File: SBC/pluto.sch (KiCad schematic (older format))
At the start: 0 parts

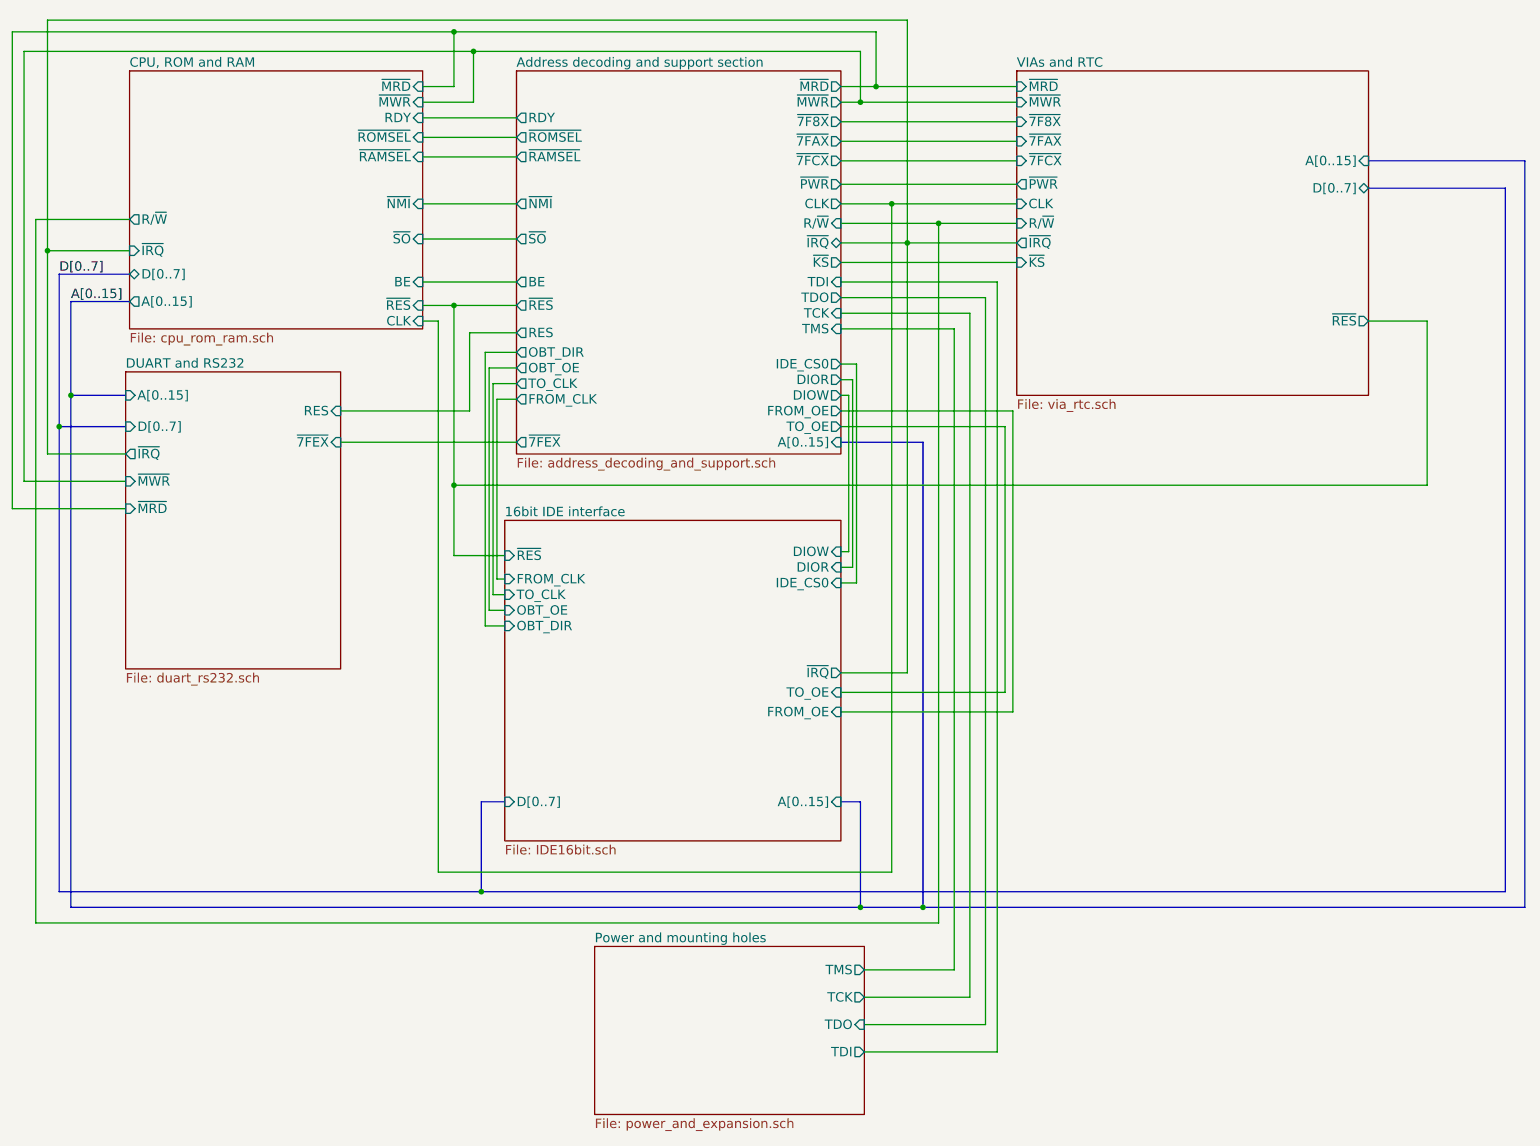
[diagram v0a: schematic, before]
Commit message: Board ready for production. Added a reset IC that does both low and high logic RES. A power switch and fuse holder is in place. The expansion bus is back, but with an IDC 40 pin connector.
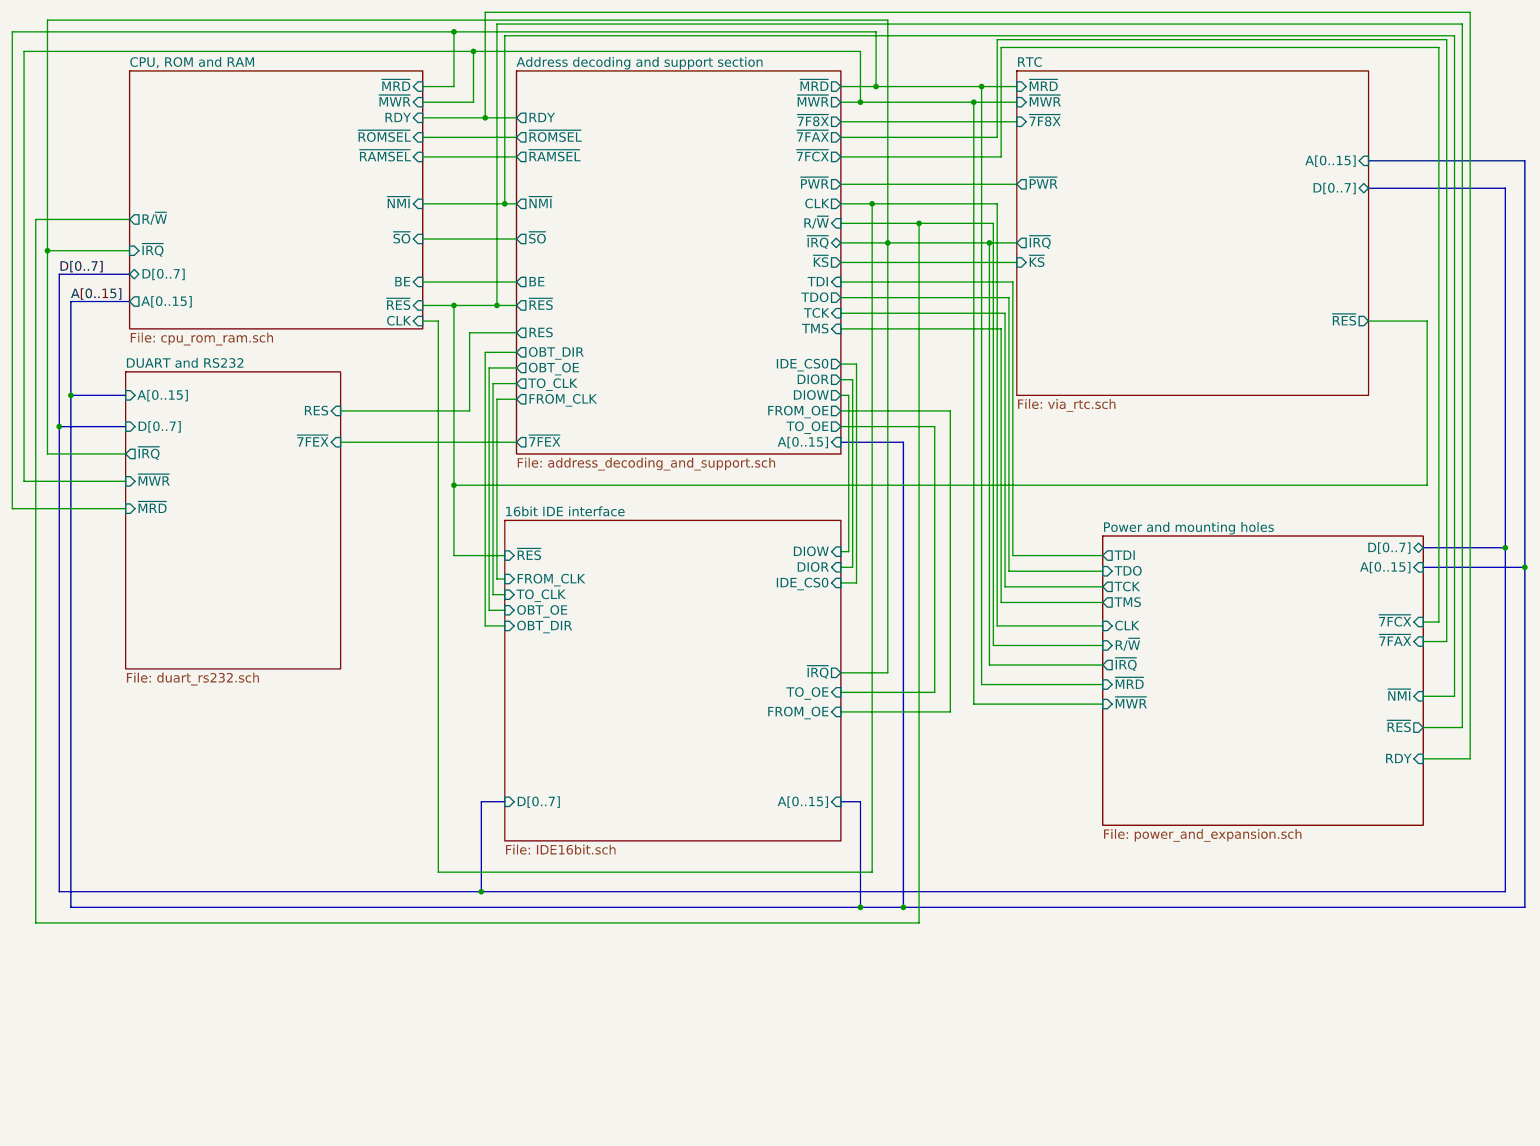
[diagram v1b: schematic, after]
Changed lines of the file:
@@
 LIBS:transistor
 LIBS:uln-ic
+LIBS:74xgxx
+LIBS:ac-dc
+LIBS:actel
+LIBS:allegro
+LIBS:Altera
+LIBS:analog_devices
+LIBS:battery_management
+LIBS:bbd
+LIBS:bosch
+LIBS:brooktre
+LIBS:cmos_ieee
+LIBS:dc-dc
+LIBS:diode
+LIBS:elec-unifil
+LIBS:ESD_Protection
+LIBS:ftdi
+LIBS:gennum
+LIBS:graphic
+LIBS:hc11
+LIBS:intersil
+LIBS:ir
+LIBS:Lattice
+LIBS:leds
+LIBS:LEM
+LIBS:logo
+LIBS:maxim
+LIBS:mechanical
+LIBS:microchip_dspic33dsc
+LIBS:microchip_pic10mcu
+LIBS:microchip_pic12mcu
+LIBS:microchip_pic16mcu
+LIBS:microchip_pic18mcu
+LIBS:microchip_pic24mcu
+LIBS:microchip_pic32mcu
+LIBS:modules
+LIBS:motor_drivers
+LIBS:motors
+LIBS:msp430
+LIBS:nordicsemi
+LIBS:nxp
+LIBS:nxp_armmcu
+LIBS:onsemi
+LIBS:Oscillators
+LIBS:powerint
+LIBS:Power_Management
+LIBS:pspice
+LIBS:references
+LIBS:relays
+LIBS:rfcom
+LIBS:RFSolutions
+LIBS:sensors
+LIBS:silabs
+LIBS:stm8
+LIBS:stm32
+LIBS:supertex
+LIBS:switches
+LIBS:transf
+LIBS:triac_thyristor
+LIBS:ttl_ieee
+LIBS:video
+LIBS:wiznet
+LIBS:Worldsemi
+LIBS:Xicor
+LIBS:zetex
+LIBS:Zilog
+LIBS:pluto
 LIBS:+1.8V
 LIBS:+3.3V
@@
 LIBS:VREG
 LIBS:VREG_VOUTCENTER
-LIBS:74xgxx
-LIBS:ac-dc
-LIBS:actel
-LIBS:allegro
-LIBS:Altera
-LIBS:analog_devices
-LIBS:battery_management
-LIBS:bbd
-LIBS:bosch
-LIBS:brooktre
-LIBS:cmos_ieee
-LIBS:dc-dc
-LIBS:diode
-LIBS:elec-unifil
-LIBS:ESD_Protection
-LIBS:ftdi
-LIBS:gennum
-LIBS:graphic
-LIBS:hc11
-LIBS:intersil
-LIBS:ir
-LIBS:Lattice
-LIBS:leds
-LIBS:LEM
-LIBS:logo
-LIBS:maxim
-LIBS:mechanical
-LIBS:microchip_dspic33dsc
-LIBS:microchip_pic10mcu
-LIBS:microchip_pic12mcu
-LIBS:microchip_pic16mcu
-LIBS:microchip_pic18mcu
-LIBS:microchip_pic24mcu
-LIBS:microchip_pic32mcu
-LIBS:modules
-LIBS:motor_drivers
-LIBS:motors
-LIBS:msp430
-LIBS:nordicsemi
-LIBS:nxp
-LIBS:nxp_armmcu
-LIBS:onsemi
-LIBS:Oscillators
-LIBS:powerint
-LIBS:Power_Management
-LIBS:pspice
-LIBS:references
-LIBS:relays
-LIBS:rfcom
-LIBS:RFSolutions
-LIBS:sensors
-LIBS:silabs
-LIBS:stm8
-LIBS:stm32
-LIBS:supertex
-LIBS:switches
-LIBS:transf
-LIBS:triac_thyristor
-LIBS:ttl_ieee
-LIBS:video
-LIBS:wiznet
-LIBS:Worldsemi
-LIBS:Xicor
-LIBS:zetex
-LIBS:Zilog
-LIBS:pluto
 LIBS:pluto-cache
 EELAYER 25 0
@@
 S 7025 900  2250 2075
 U 58D58980
-F0 "VIAs and RTC" 60
+F0 "RTC" 60
 F1 "via_rtc.sch" 60
 F2 "D[0..7]" B R 9275 1650 60
-F3 "~7FCX" I L 7025 1475 60
-F4 "A[0..15]" I R 9275 1475 60
-F5 "~PWR" O L 7025 1625 60
-F6 "~RES" O R 9275 2500 60
-F7 "~IRQ" O L 7025 2000 60
-F8 "~MWR" I L 7025 1100 60
-F9 "~MRD" I L 7025 1000 60
-F10 "~7F8X" I L 7025 1225 60
-F11 "~7FAX" I L 7025 1350 60
-F12 "R/~W" I L 7025 1875 60
-F13 "CLK" I L 7025 1750 60
-F14 "~KS" I L 7025 2125 60
+F3 "A[0..15]" I R 9275 1475 60
+F4 "~PWR" O L 7025 1625 60
+F5 "~RES" O R 9275 2500 60
+F6 "~IRQ" O L 7025 2000 60
+F7 "~MWR" I L 7025 1100 60
+F8 "~MRD" I L 7025 1000 60
+F9 "~7F8X" I L 7025 1225 60
+F10 "~KS" I L 7025 2125 60
 $EndSheet
 $Sheet
@@
 F14 "~RES" O L 3825 2400 60
 F15 "~7F8X" O R 5900 1225 60
-F16 "~7FAX" O R 5900 1350 60
-F17 "~7FCX" O R 5900 1475 60
-F18 "~7FEX" O L 3825 3275 60
-F19 "~KS" O R 5900 2125 60
-F20 "~SO" O L 3825 1975 60
-F21 "RES" O L 3825 2575 60
-F22 "TDI" I R 5900 2250 60
-F23 "TDO" O R 5900 2350 60
-F24 "TCK" I R 5900 2450 60
-F25 "TMS" I R 5900 2550 60
-F26 "FROM_OE" O R 5900 3075 60
-F27 "FROM_CLK" O L 3825 3000 60
-F28 "TO_OE" O R 5900 3175 60
-F29 "TO_CLK" O L 3825 2900 60
-F30 "OBT_OE" O L 3825 2800 60
-F31 "OBT_DIR" O L 3825 2700 60
-F32 "DIOR" O R 5900 2875 60
-F33 "DIOW" O R 5900 2975 60
-F34 "IDE_CS0" O R 5900 2775 60
+F16 "~7FEX" O L 3825 3275 60
+F17 "~KS" O R 5900 2125 60
+F18 "~SO" O L 3825 1975 60
+F19 "RES" O L 3825 2575 60
+F20 "TDI" I R 5900 2250 60
+F21 "TDO" O R 5900 2350 60
+F22 "TCK" I R 5900 2450 60
+F23 "TMS" I R 5900 2550 60
+F24 "FROM_OE" O R 5900 3075 60
+F25 "FROM_CLK" O L 3825 3000 60
+F26 "TO_OE" O R 5900 3175 60
+F27 "TO_CLK" O L 3825 2900 60
+F28 "OBT_OE" O L 3825 2800 60
+F29 "OBT_DIR" O L 3825 2700 60
+F30 "DIOR" O R 5900 2875 60
+F31 "DIOW" O R 5900 2975 60
+F32 "IDE_CS0" O R 5900 2775 60
+F33 "~7FAX" O R 5900 1325 60
+F34 "~7FCX" O R 5900 1450 60
 $EndSheet
 $Sheet
-S 4325 6500 1725 1075
+S 7575 3875 2050 1850
 U 58D589DC
 F0 "Power and mounting holes" 60
 F1 "power_and_expansion.sch" 60
-F2 "TDI" O R 6050 7175 60
-F3 "TDO" I R 6050 7000 60
-F4 "TCK" O R 6050 6825 60
-F5 "TMS" O R 6050 6650 60
+F2 "TDI" O L 7575 4000 60
+F3 "TDO" I L 7575 4100 60
+F4 "TCK" O L 7575 4200 60
+F5 "TMS" O L 7575 4300 60
+F6 "~7FAX" I R 9625 4550 60
+F7 "~7FCX" I R 9625 4425 60
+F8 "~IRQ" O L 7575 4700 60
+F9 "~RES" O R 9625 5100 60
+F10 "~MRD" I L 7575 4825 60
+F11 "~MWR" I L 7575 4950 60
+F12 "R/~W" I L 7575 4575 60
+F13 "CLK" I L 7575 4450 60
+F14 "~NMI" I R 9625 4900 60
+F15 "RDY" I R 9625 5300 60
+F16 "D[0..7]" B R 9625 3950 60
+F17 "A[0..15]" I R 9625 4075 60
 $EndSheet
 $Sheet
@@
 	5900 2000 7025 2000
 Wire Wire Line
-	5900 1875 7025 1875
-Wire Wire Line
 	5900 1000 7025 1000
 Wire Wire Line
@@
 Wire Wire Line
 	5900 1625 7025 1625
-Wire Wire Line
-	5900 1750 7025 1750
 Wire Wire Line
 	3225 1000 3425 1000
@@
 Wire Wire Line
 	5900 1225 7025 1225
-Wire Wire Line
-	5900 1350 7025 1350
-Wire Wire Line
-	5900 1475 7025 1475
 Wire Wire Line
 	9275 2500 9650 2500
@@
 Connection ~ 6025 6250
 Wire Wire Line
-	6225 1750 6225 6025
-Connection ~ 6225 1750
-Wire Wire Line
-	825  575  6325 575
-Wire Wire Line
-	6325 575  6325 4750
-Connection ~ 6325 2000
+	6100 1750 6100 6025
+Wire Wire Line
+	825  575  6200 575
+Wire Wire Line
+	6200 575  6200 4750
+Connection ~ 6200 2000
 Connection ~ 825  2050
 Wire Wire Line
-	6325 4750 5900 4750
+	6200 4750 5900 4750
 Connection ~ 3425 2400
 Wire Wire Line
@@
 	3225 1750 3825 1750
 Wire Bus Line
-	5900 3275 6425 3275
-Wire Bus Line
-	6425 3275 6425 6250
-Connection ~ 6425 6250
-Wire Wire Line
-	750  6350 6525 6350
-Wire Wire Line
-	6525 6350 6525 1875
-Connection ~ 6525 1875
-Wire Wire Line
-	6225 6025 3325 6025
+	5900 3275 6300 3275
+Wire Bus Line
+	6300 3275 6300 6250
+Connection ~ 6300 6250
+Wire Wire Line
+	750  6350 6400 6350
+Wire Wire Line
+	6400 6350 6400 1875
+Wire Wire Line
+	6100 6025 3325 6025
 Wire Wire Line
 	7025 2125 5900 2125
@@
 	3525 3075 2700 3075
 Wire Wire Line
-	5900 2550 6625 2550
-Wire Wire Line
-	6625 2550 6625 6650
-Wire Wire Line
-	6625 6650 6050 6650
-Wire Wire Line
-	5900 2450 6725 2450
-Wire Wire Line
-	6725 2450 6725 6825
-Wire Wire Line
-	6725 6825 6050 6825
-Wire Wire Line
-	5900 2350 6825 2350
-Wire Wire Line
-	6825 2350 6825 7000
-Wire Wire Line
-	6825 7000 6050 7000
-Wire Wire Line
-	5900 2250 6900 2250
-Wire Wire Line
-	6900 2250 6900 7175
-Wire Wire Line
-	6900 7175 6050 7175
-Wire Wire Line
-	5900 3175 6950 3175
-Wire Wire Line
-	6950 3175 6950 4875
-Wire Wire Line
-	6950 4875 5900 4875
-Wire Wire Line
-	5900 3075 7000 3075
-Wire Wire Line
-	7000 3075 7000 5000
-Wire Wire Line
-	7000 5000 5900 5000
+	5900 3175 6500 3175
+Wire Wire Line
+	6500 3175 6500 4875
+Wire Wire Line
+	6500 4875 5900 4875
+Wire Wire Line
+	5900 3075 6600 3075
+Wire Wire Line
+	6600 3075 6600 5000
+Wire Wire Line
+	6600 5000 5900 5000
 Wire Wire Line
 	3825 3000 3700 3000
@@
 Wire Wire Line
 	9650 3550 9650 2500
+Wire Wire Line
+	5900 1750 6900 1750
+Wire Wire Line
+	5900 1875 6875 1875
+Wire Wire Line
+	5900 1450 6925 1450
+Wire Wire Line
+	5900 1325 6900 1325
+Wire Wire Line
+	5900 2550 6925 2550
+Wire Wire Line
+	6925 2550 6925 4300
+Wire Wire Line
+	6925 4300 7575 4300
+Wire Wire Line
+	7575 4200 6950 4200
+Wire Wire Line
+	6950 4200 6950 2450
+Wire Wire Line
+	6950 2450 5900 2450
+Wire Wire Line
+	5900 2350 6975 2350
+Wire Wire Line
+	6975 2350 6975 4100
+Wire Wire Line
+	6975 4100 7575 4100
+Wire Wire Line
+	7000 4000 7575 4000
+Wire Wire Line
+	7000 2250 7000 4000
+Wire Wire Line
+	7000 2250 5900 2250
+Wire Bus Line
+	9625 3950 10150 3950
+Wire Bus Line
+	9625 4075 10275 4075
+Connection ~ 10275 4075
+Connection ~ 10150 3950
+Wire Wire Line
+	6925 1450 6925 750
+Wire Wire Line
+	6925 750  9725 750
+Wire Wire Line
+	9725 750  9725 4425
+Wire Wire Line
+	9725 4425 9625 4425
+Wire Wire Line
+	6900 1325 6900 700
+Wire Wire Line
+	6900 700  9775 700
+Wire Wire Line
+	9775 700  9775 4550
+Wire Wire Line
+	9775 4550 9625 4550
+Wire Wire Line
+	6900 1750 6900 4450
+Wire Wire Line
+	6900 4450 7575 4450
+Connection ~ 6100 1750
+Wire Wire Line
+	6875 1875 6875 4575
+Wire Wire Line
+	6875 4575 7575 4575
+Connection ~ 6400 1875
+Wire Wire Line
+	7575 4700 6850 4700
+Wire Wire Line
+	6850 4700 6850 2000
+Connection ~ 6850 2000
+Wire Wire Line
+	7575 4825 6800 4825
+Wire Wire Line
+	6800 4825 6800 1000
+Connection ~ 6800 1000
+Wire Wire Line
+	7575 4950 6750 4950
+Wire Wire Line
+	6750 4950 6750 1100
+Connection ~ 6750 1100
+Wire Wire Line
+	3750 1750 3750 675
+Wire Wire Line
+	3750 675  9825 675
+Wire Wire Line
+	9825 675  9825 4900
+Wire Wire Line
+	9825 4900 9625 4900
+Connection ~ 3750 1750
+Wire Wire Line
+	9625 5100 9875 5100
+Wire Wire Line
+	9875 5100 9875 600
+Wire Wire Line
+	9875 600  3700 600
+Wire Wire Line
+	3700 600  3700 2400
+Connection ~ 3700 2400
+Wire Wire Line
+	9625 5300 9925 5300
+Wire Wire Line
+	9925 5300 9925 525
+Wire Wire Line
+	9925 525  3625 525
+Wire Wire Line
+	3625 525  3625 1200
+Connection ~ 3625 1200
 $EndSCHEMATC
